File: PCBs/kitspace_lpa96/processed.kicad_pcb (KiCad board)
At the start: 4 copper layers, 143 x 74 mm, 161 parts, among them IC1 ATMEGA328-A, P1 CONN_2, P2 CONN_3X2, SW1 SW_PUSH, U1 SD_CARD, U2 LD1117S33, U3 TLC5941, U4 TLC5941, U5 TLC5941, U6 TLC5941, U7 TLC5941, U8 TLC5941, Y1 RESONATEUR

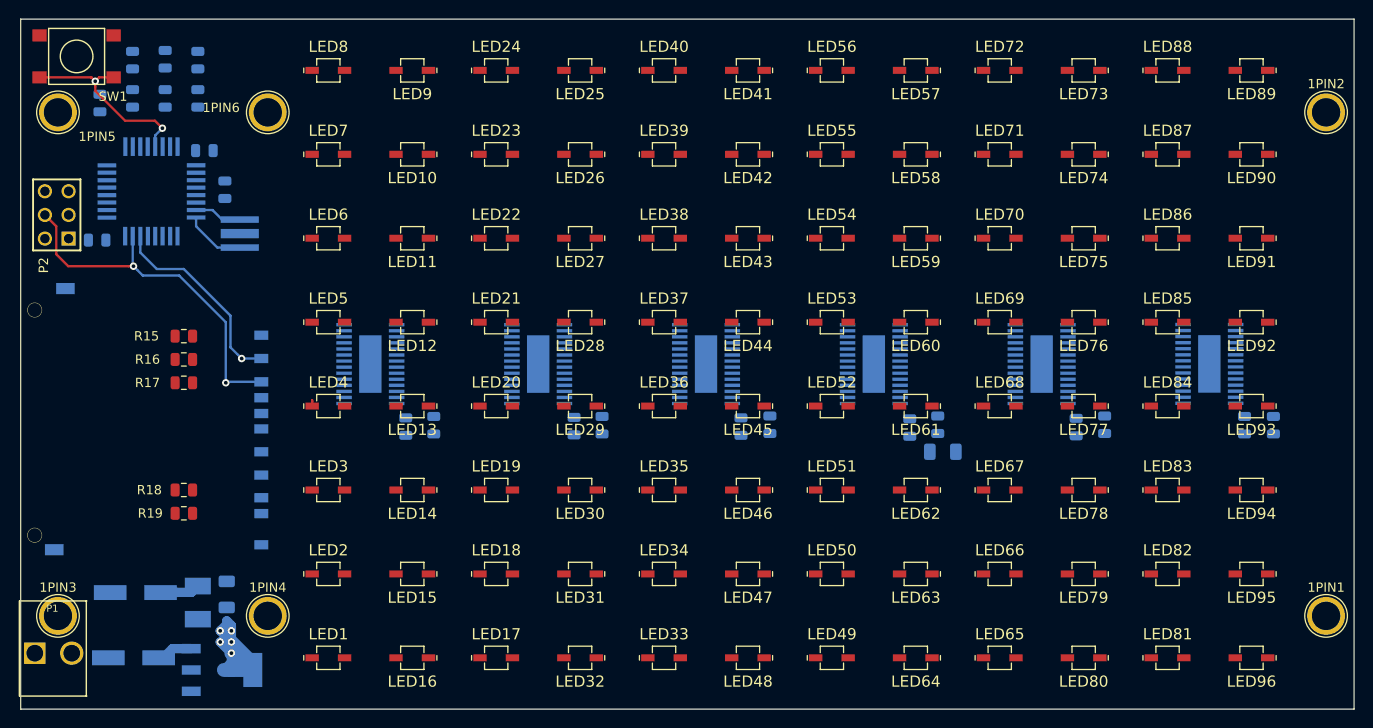
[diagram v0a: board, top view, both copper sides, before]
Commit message: recheck all circuits and clean up fill zone by rerouting the nets using freerouting and manually
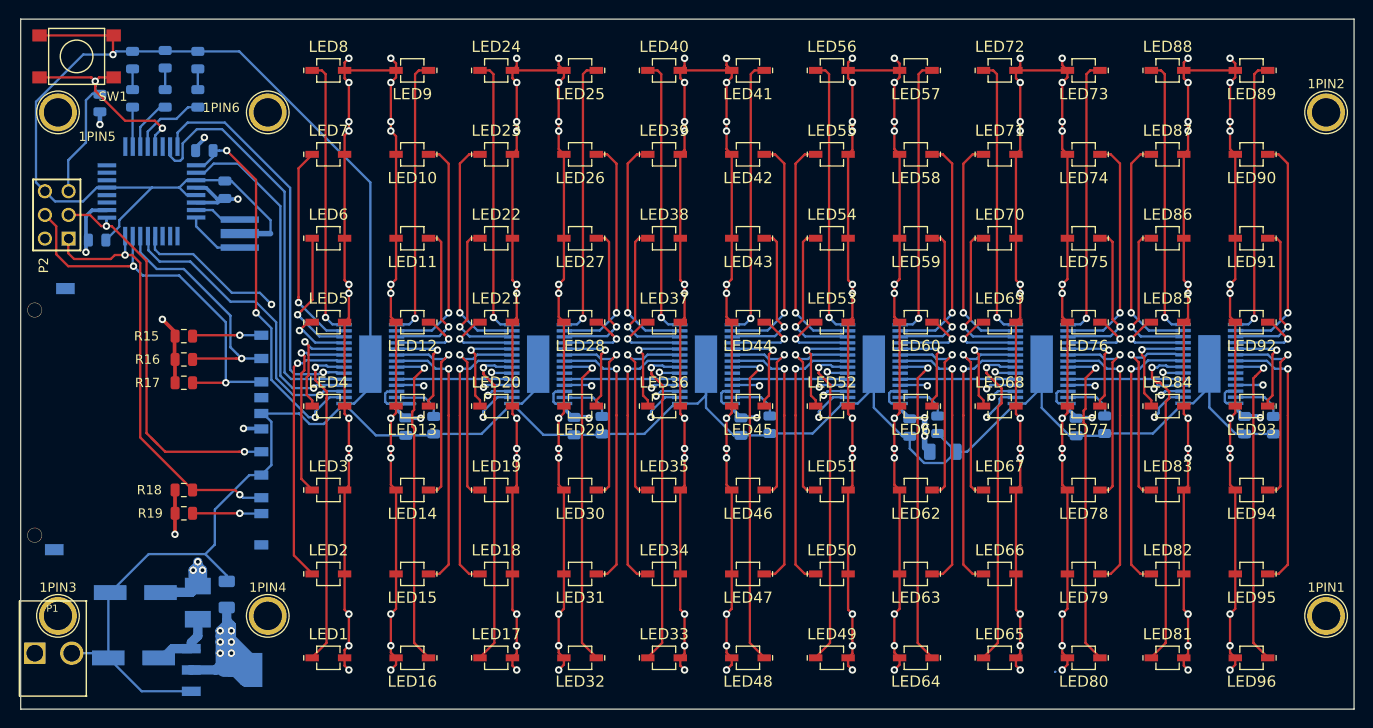
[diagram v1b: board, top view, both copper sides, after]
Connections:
- C1 pad 1: (no net) -> GND
- C1 pad 2: (no net) -> VCC
- C10 pad 1: (no net) -> VCC
- C10 pad 2: (no net) -> GND
- C11 pad 1: (no net) -> VCC
- C11 pad 2: (no net) -> GND
- C12 pad 1: (no net) -> VCC
- C12 pad 2: (no net) -> GND
- C2 pad 1: (no net) -> GND
- C2 pad 2: (no net) -> VCC
- C3 pad 2: (no net) -> GND
- C4 pad 2: (no net) -> GND
- C5 pad 1: (no net) -> VCC
- C5 pad 2: (no net) -> GND
- C6 pad 1: (no net) -> VCC
- C6 pad 2: (no net) -> GND
- C7 pad 1: (no net) -> VCC
- C7 pad 2: (no net) -> GND
- C8 pad 1: (no net) -> VCC
- C8 pad 2: (no net) -> GND
- C9 pad 1: (no net) -> VCC
- C9 pad 2: (no net) -> GND
- IC1 pad 1: (no net) -> /BLANK
- IC1 pad 10: (no net) -> Net-(IC1-Pad10)
- IC1 pad 11: (no net) -> Net-(IC1-Pad11)
- IC1 pad 12: (no net) -> /GSCLK
- IC1 pad 13: (no net) -> /XLAT
- IC1 pad 16: (no net) -> /MISO
- IC1 pad 17: (no net) -> /SCK
- IC1 pad 18: (no net) -> VCC
- IC1 pad 19: (no net) -> Net-(IC1-Pad19)
- IC1 pad 2: (no net) -> /SCLK
- IC1 pad 20: (no net) -> Net-(IC1-Pad20)
- IC1 pad 21: (no net) -> GND
- IC1 pad 22: (no net) -> Net-(IC1-Pad22)
- IC1 pad 23: (no net) -> Net-(IC1-Pad23)
- IC1 pad 24: (no net) -> Net-(IC1-Pad24)
- IC1 pad 25: (no net) -> Net-(IC1-Pad25)
- IC1 pad 26: (no net) -> /ON
- IC1 pad 27: (no net) -> /ERR
- IC1 pad 28: (no net) -> /FIN
- IC1 pad 3: (no net) -> GND
- IC1 pad 30: (no net) -> Net-(IC1-Pad30)
- IC1 pad 31: (no net) -> /SIN
- IC1 pad 32: (no net) -> /MODE
- IC1 pad 4: (no net) -> VCC
- IC1 pad 5: (no net) -> GND
- IC1 pad 6: (no net) -> VCC
- IC1 pad 9: (no net) -> Net-(IC1-Pad9)
- L1 pad 2: (no net) -> Net-(C4-Pad1)
- LED1 pad 1: (no net) -> Net-(LED1-Pad1)
- LED1 pad 2: (no net) -> /VIN
- LED10 pad 1: (no net) -> Net-(LED10-Pad1)
- LED10 pad 2: (no net) -> /VIN
- LED11 pad 1: (no net) -> Net-(LED11-Pad1)
- LED11 pad 2: (no net) -> /VIN
- LED12 pad 1: (no net) -> Net-(LED12-Pad1)
- LED12 pad 2: (no net) -> /VIN
- LED13 pad 1: (no net) -> Net-(LED13-Pad1)
- LED13 pad 2: (no net) -> /VIN
- LED14 pad 1: (no net) -> Net-(LED14-Pad1)
- LED14 pad 2: (no net) -> /VIN
- LED15 pad 1: (no net) -> Net-(LED15-Pad1)
- LED15 pad 2: (no net) -> /VIN
- LED16 pad 1: (no net) -> Net-(LED16-Pad1)
- LED16 pad 2: (no net) -> /VIN
- LED17 pad 1: (no net) -> Net-(LED17-Pad1)
- LED17 pad 2: (no net) -> /VIN
- LED18 pad 1: (no net) -> Net-(LED18-Pad1)
- LED18 pad 2: (no net) -> /VIN
- LED19 pad 1: (no net) -> Net-(LED19-Pad1)
- LED19 pad 2: (no net) -> /VIN
- LED2 pad 1: (no net) -> Net-(LED2-Pad1)
- LED2 pad 2: (no net) -> /VIN
- LED20 pad 1: (no net) -> Net-(LED20-Pad1)
- LED20 pad 2: (no net) -> /VIN
- LED21 pad 1: (no net) -> Net-(LED21-Pad1)
- LED21 pad 2: (no net) -> /VIN
- LED22 pad 1: (no net) -> Net-(LED22-Pad1)
- LED22 pad 2: (no net) -> /VIN
- LED23 pad 1: (no net) -> Net-(LED23-Pad1)
- LED23 pad 2: (no net) -> /VIN
- LED24 pad 1: (no net) -> Net-(LED24-Pad1)
- LED24 pad 2: (no net) -> /VIN
- LED25 pad 1: (no net) -> Net-(LED25-Pad1)
- LED25 pad 2: (no net) -> /VIN
- LED26 pad 1: (no net) -> Net-(LED26-Pad1)
- LED26 pad 2: (no net) -> /VIN
- LED27 pad 1: (no net) -> Net-(LED27-Pad1)
- LED27 pad 2: (no net) -> /VIN
- LED28 pad 1: (no net) -> Net-(LED28-Pad1)
- LED28 pad 2: (no net) -> /VIN
- LED29 pad 1: (no net) -> Net-(LED29-Pad1)
- LED29 pad 2: (no net) -> /VIN
- LED3 pad 1: (no net) -> Net-(LED3-Pad1)
- LED3 pad 2: (no net) -> /VIN
- LED30 pad 1: (no net) -> Net-(LED30-Pad1)
- LED30 pad 2: (no net) -> /VIN
- LED31 pad 1: (no net) -> Net-(LED31-Pad1)
- LED31 pad 2: (no net) -> /VIN
- LED32 pad 1: (no net) -> Net-(LED32-Pad1)
- LED32 pad 2: (no net) -> /VIN
- LED33 pad 1: (no net) -> Net-(LED33-Pad1)
- LED33 pad 2: (no net) -> /VIN
- LED34 pad 1: (no net) -> Net-(LED34-Pad1)
- LED34 pad 2: (no net) -> /VIN
- LED35 pad 1: (no net) -> Net-(LED35-Pad1)
- LED35 pad 2: (no net) -> /VIN
- LED36 pad 1: (no net) -> Net-(LED36-Pad1)
- LED36 pad 2: (no net) -> /VIN
- LED37 pad 1: (no net) -> Net-(LED37-Pad1)
- LED37 pad 2: (no net) -> /VIN
- LED38 pad 1: (no net) -> Net-(LED38-Pad1)
- LED38 pad 2: (no net) -> /VIN
- LED39 pad 1: (no net) -> Net-(LED39-Pad1)
- LED39 pad 2: (no net) -> /VIN
- LED4 pad 2: (no net) -> /VIN
- LED40 pad 1: (no net) -> Net-(LED40-Pad1)
- LED40 pad 2: (no net) -> /VIN
- LED41 pad 1: (no net) -> Net-(LED41-Pad1)
- LED41 pad 2: (no net) -> /VIN
- LED42 pad 1: (no net) -> Net-(LED42-Pad1)
- LED42 pad 2: (no net) -> /VIN
- LED43 pad 1: (no net) -> Net-(LED43-Pad1)
- LED43 pad 2: (no net) -> /VIN
- LED44 pad 1: (no net) -> Net-(LED44-Pad1)
- LED44 pad 2: (no net) -> /VIN
- LED45 pad 1: (no net) -> Net-(LED45-Pad1)
- LED45 pad 2: (no net) -> /VIN
- LED46 pad 1: (no net) -> Net-(LED46-Pad1)
- LED46 pad 2: (no net) -> /VIN
- LED47 pad 1: (no net) -> Net-(LED47-Pad1)
- LED47 pad 2: (no net) -> /VIN
- LED48 pad 1: (no net) -> Net-(LED48-Pad1)
- LED48 pad 2: (no net) -> /VIN
- LED49 pad 1: (no net) -> Net-(LED49-Pad1)
- LED49 pad 2: (no net) -> /VIN
- LED5 pad 1: (no net) -> Net-(LED5-Pad1)
- LED5 pad 2: (no net) -> /VIN
- LED50 pad 1: (no net) -> Net-(LED50-Pad1)
- LED50 pad 2: (no net) -> /VIN
- LED51 pad 1: (no net) -> Net-(LED51-Pad1)
- LED51 pad 2: (no net) -> /VIN
- LED52 pad 1: (no net) -> Net-(LED52-Pad1)
- LED52 pad 2: (no net) -> /VIN
- LED53 pad 1: (no net) -> Net-(LED53-Pad1)
- LED53 pad 2: (no net) -> /VIN
- LED54 pad 1: (no net) -> Net-(LED54-Pad1)
- LED54 pad 2: (no net) -> /VIN
- LED55 pad 1: (no net) -> Net-(LED55-Pad1)
- LED55 pad 2: (no net) -> /VIN
- LED56 pad 1: (no net) -> Net-(LED56-Pad1)
- LED56 pad 2: (no net) -> /VIN
- LED57 pad 1: (no net) -> Net-(LED57-Pad1)
- LED57 pad 2: (no net) -> /VIN
- LED58 pad 1: (no net) -> Net-(LED58-Pad1)
- LED58 pad 2: (no net) -> /VIN
- LED59 pad 1: (no net) -> Net-(LED59-Pad1)
- LED59 pad 2: (no net) -> /VIN
- LED6 pad 1: (no net) -> Net-(LED6-Pad1)
- LED6 pad 2: (no net) -> /VIN
- LED60 pad 1: (no net) -> Net-(LED60-Pad1)
- LED60 pad 2: (no net) -> /VIN
- LED61 pad 1: (no net) -> Net-(LED61-Pad1)
- LED61 pad 2: (no net) -> /VIN
- LED62 pad 1: (no net) -> Net-(LED62-Pad1)
- LED62 pad 2: (no net) -> /VIN
- LED63 pad 1: (no net) -> Net-(LED63-Pad1)
- LED63 pad 2: (no net) -> /VIN
- LED64 pad 1: (no net) -> Net-(LED64-Pad1)
- LED64 pad 2: (no net) -> /VIN
- LED65 pad 1: (no net) -> Net-(LED65-Pad1)
- LED65 pad 2: (no net) -> /VIN
- LED66 pad 1: (no net) -> Net-(LED66-Pad1)
- LED66 pad 2: (no net) -> /VIN
- LED67 pad 1: (no net) -> Net-(LED67-Pad1)
- LED67 pad 2: (no net) -> /VIN
- LED68 pad 1: (no net) -> Net-(LED68-Pad1)
- LED68 pad 2: (no net) -> /VIN
- LED69 pad 1: (no net) -> Net-(LED69-Pad1)
- LED69 pad 2: (no net) -> /VIN
- LED7 pad 1: (no net) -> Net-(LED7-Pad1)
- LED7 pad 2: (no net) -> /VIN
- LED70 pad 1: (no net) -> Net-(LED70-Pad1)
- LED70 pad 2: (no net) -> /VIN
- LED71 pad 1: (no net) -> Net-(LED71-Pad1)
- LED71 pad 2: (no net) -> /VIN
- LED72 pad 1: (no net) -> Net-(LED72-Pad1)
- LED72 pad 2: (no net) -> /VIN
- LED73 pad 1: (no net) -> Net-(LED73-Pad1)
- LED73 pad 2: (no net) -> /VIN
- LED74 pad 1: (no net) -> Net-(LED74-Pad1)
- LED74 pad 2: (no net) -> /VIN
- LED75 pad 1: (no net) -> Net-(LED75-Pad1)
- LED75 pad 2: (no net) -> /VIN
- LED76 pad 1: (no net) -> Net-(LED76-Pad1)
- LED76 pad 2: (no net) -> /VIN
- LED77 pad 1: (no net) -> Net-(LED77-Pad1)
- LED77 pad 2: (no net) -> /VIN
- LED78 pad 1: (no net) -> Net-(LED78-Pad1)
- LED78 pad 2: (no net) -> /VIN
- LED79 pad 1: (no net) -> Net-(LED79-Pad1)
- LED79 pad 2: (no net) -> /VIN
- LED8 pad 1: (no net) -> Net-(LED8-Pad1)
- LED8 pad 2: (no net) -> /VIN
- LED80 pad 1: (no net) -> Net-(LED80-Pad1)
- LED80 pad 2: (no net) -> /VIN
- LED81 pad 1: (no net) -> Net-(LED81-Pad1)
- LED81 pad 2: (no net) -> /VIN
- LED82 pad 1: (no net) -> Net-(LED82-Pad1)
- LED82 pad 2: (no net) -> /VIN
- LED83 pad 1: (no net) -> Net-(LED83-Pad1)
- LED83 pad 2: (no net) -> /VIN
- LED84 pad 1: (no net) -> Net-(LED84-Pad1)
- LED84 pad 2: (no net) -> /VIN
- LED85 pad 1: (no net) -> Net-(LED85-Pad1)
- LED85 pad 2: (no net) -> /VIN
- LED86 pad 1: (no net) -> Net-(LED86-Pad1)
- LED86 pad 2: (no net) -> /VIN
- LED87 pad 1: (no net) -> Net-(LED87-Pad1)
- LED87 pad 2: (no net) -> /VIN
- LED88 pad 1: (no net) -> Net-(LED88-Pad1)
- LED88 pad 2: (no net) -> /VIN
- LED89 pad 1: (no net) -> Net-(LED89-Pad1)
- LED89 pad 2: (no net) -> /VIN
- LED9 pad 1: (no net) -> Net-(LED9-Pad1)
- LED9 pad 2: (no net) -> /VIN
- LED90 pad 1: (no net) -> Net-(LED90-Pad1)
- LED90 pad 2: (no net) -> /VIN
- LED91 pad 1: (no net) -> Net-(LED91-Pad1)
- LED91 pad 2: (no net) -> /VIN
- LED92 pad 1: (no net) -> Net-(LED92-Pad1)
- LED92 pad 2: (no net) -> /VIN
- LED93 pad 1: (no net) -> Net-(LED93-Pad1)
- LED93 pad 2: (no net) -> /VIN
- LED94 pad 1: (no net) -> Net-(LED94-Pad1)
- LED94 pad 2: (no net) -> /VIN
- LED95 pad 1: (no net) -> Net-(LED95-Pad1)
- LED95 pad 2: (no net) -> /VIN
- LED96 pad 1: (no net) -> Net-(LED96-Pad1)
- LED96 pad 2: (no net) -> /VIN
- LED97 pad 1: (no net) -> GND
- LED97 pad 2: (no net) -> Net-(LED97-Pad2)
- LED98 pad 1: (no net) -> GND
- LED98 pad 2: (no net) -> Net-(LED98-Pad2)
- LED99 pad 1: (no net) -> GND
- LED99 pad 2: (no net) -> Net-(LED99-Pad2)
- P1 pad 1: (no net) -> /VIN
- P1 pad 2: (no net) -> GND
- P2 pad 1: (no net) -> /MISO
- P2 pad 2: (no net) -> VCC
- P2 pad 3: (no net) -> /SCK
- P2 pad 5: (no net) -> /RST
- P2 pad 6: (no net) -> GND
- R1 pad 1: (no net) -> /RST
- R1 pad 2: (no net) -> VCC
- R10 pad 1: (no net) -> /ERR
- R10 pad 2: (no net) -> Net-(LED98-Pad2)
- R11 pad 1: (no net) -> /FIN
- R11 pad 2: (no net) -> Net-(LED99-Pad2)
- R15 pad 1: (no net) -> VCC
- R15 pad 2: (no net) -> Net-(R15-Pad2)
- R16 pad 1: (no net) -> VCC
- R16 pad 2: (no net) -> /SS
- R17 pad 1: (no net) -> VCC
- R17 pad 2: (no net) -> /MOSI
- R18 pad 1: (no net) -> VCC
- R18 pad 2: (no net) -> /MISO
- R19 pad 1: (no net) -> VCC
- R19 pad 2: (no net) -> Net-(R19-Pad2)
- R2 pad 1: (no net) -> /BLANK
- R2 pad 2: (no net) -> VCC
- R3 pad 1: (no net) -> GND
- R3 pad 2: (no net) -> Net-(R3-Pad2)
- R4 pad 1: (no net) -> GND
- R4 pad 2: (no net) -> Net-(R4-Pad2)
- R5 pad 1: (no net) -> GND
- R5 pad 2: (no net) -> Net-(R5-Pad2)
- R6 pad 1: (no net) -> GND
- R6 pad 2: (no net) -> Net-(R6-Pad2)
- R7 pad 1: (no net) -> GND
- R7 pad 2: (no net) -> Net-(R7-Pad2)
- R8 pad 1: (no net) -> GND
- R8 pad 2: (no net) -> Net-(R8-Pad2)
- R9 pad 1: (no net) -> /ON
- R9 pad 2: (no net) -> Net-(LED97-Pad2)
- SW1 pad 2: (no net) -> GND
- U1 pad 3: (no net) -> GND
- U1 pad 4: (no net) -> VCC
- U1 pad 5: (no net) -> /SCK
- U1 pad 6: (no net) -> GND
- U1 pad 7: (no net) -> /MISO
- U1 pad 8: (no net) -> Net-(R19-Pad2)
- U1 pad 9: (no net) -> Net-(R15-Pad2)
- U2 pad 1: (no net) -> GND
- U2 pad 2: (no net) -> VCC
- U3 pad 1: (no net) -> GND
- U3 pad 10: (no net) -> Net-(LED4-Pad1)
- U3 pad 11: (no net) -> Net-(LED5-Pad1)
- U3 pad 12: (no net) -> Net-(LED6-Pad1)
- U3 pad 13: (no net) -> Net-(LED7-Pad1)
- U3 pad 14: (no net) -> Net-(LED8-Pad1)
- U3 pad 15: (no net) -> Net-(LED9-Pad1)
- U3 pad 16: (no net) -> Net-(LED10-Pad1)
- U3 pad 17: (no net) -> Net-(LED11-Pad1)
- U3 pad 18: (no net) -> Net-(LED12-Pad1)
- U3 pad 19: (no net) -> Net-(LED13-Pad1)
- U3 pad 2: (no net) -> /BLANK
- U3 pad 20: (no net) -> Net-(LED14-Pad1)
- U3 pad 21: (no net) -> Net-(LED15-Pad1)
- U3 pad 22: (no net) -> Net-(LED16-Pad1)
- U3 pad 23: (no net) -> Net-(U3-Pad23)
- U3 pad 24: (no net) -> /lpa96_leds_drivers/SOUT1
- U3 pad 25: (no net) -> /GSCLK
- U3 pad 26: (no net) -> VCC
- U3 pad 27: (no net) -> Net-(R3-Pad2)
- U3 pad 28: (no net) -> VCC
- U3 pad 29: (no net) -> GND
- U3 pad 3: (no net) -> /XLAT
- U3 pad 4: (no net) -> /SCLK
- U3 pad 5: (no net) -> /SIN
- U3 pad 6: (no net) -> /MODE
- U3 pad 7: (no net) -> Net-(LED1-Pad1)
- U3 pad 8: (no net) -> Net-(LED2-Pad1)
- U3 pad 9: (no net) -> Net-(LED3-Pad1)
- U4 pad 1: (no net) -> GND
- U4 pad 10: (no net) -> Net-(LED20-Pad1)
- U4 pad 11: (no net) -> Net-(LED21-Pad1)
- U4 pad 12: (no net) -> Net-(LED22-Pad1)
- U4 pad 13: (no net) -> Net-(LED23-Pad1)
- U4 pad 14: (no net) -> Net-(LED24-Pad1)
- U4 pad 15: (no net) -> Net-(LED25-Pad1)
- U4 pad 16: (no net) -> Net-(LED26-Pad1)
- U4 pad 17: (no net) -> Net-(LED27-Pad1)
- U4 pad 18: (no net) -> Net-(LED28-Pad1)
- U4 pad 19: (no net) -> Net-(LED29-Pad1)
- U4 pad 2: (no net) -> /BLANK
- U4 pad 20: (no net) -> Net-(LED30-Pad1)
- U4 pad 21: (no net) -> Net-(LED31-Pad1)
- U4 pad 22: (no net) -> Net-(LED32-Pad1)
- U4 pad 23: (no net) -> Net-(U4-Pad23)
- U4 pad 24: (no net) -> /lpa96_leds_drivers/SOUT2
- U4 pad 25: (no net) -> /GSCLK
- U4 pad 26: (no net) -> VCC
- U4 pad 27: (no net) -> Net-(R4-Pad2)
- U4 pad 28: (no net) -> VCC
- U4 pad 29: (no net) -> GND
- U4 pad 3: (no net) -> /XLAT
- U4 pad 4: (no net) -> /SCLK
- U4 pad 5: (no net) -> /lpa96_leds_drivers/SOUT1
- U4 pad 6: (no net) -> /MODE
- U4 pad 7: (no net) -> Net-(LED17-Pad1)
- U4 pad 8: (no net) -> Net-(LED18-Pad1)
- U4 pad 9: (no net) -> Net-(LED19-Pad1)
- U5 pad 1: (no net) -> GND
- U5 pad 10: (no net) -> Net-(LED36-Pad1)
- U5 pad 11: (no net) -> Net-(LED37-Pad1)
- U5 pad 12: (no net) -> Net-(LED38-Pad1)
- U5 pad 13: (no net) -> Net-(LED39-Pad1)
- U5 pad 14: (no net) -> Net-(LED40-Pad1)
- U5 pad 15: (no net) -> Net-(LED41-Pad1)
- U5 pad 16: (no net) -> Net-(LED42-Pad1)
- U5 pad 17: (no net) -> Net-(LED43-Pad1)
- U5 pad 18: (no net) -> Net-(LED44-Pad1)
- U5 pad 19: (no net) -> Net-(LED45-Pad1)
- U5 pad 2: (no net) -> /BLANK
- U5 pad 20: (no net) -> Net-(LED46-Pad1)
- U5 pad 21: (no net) -> Net-(LED47-Pad1)
- U5 pad 22: (no net) -> Net-(LED48-Pad1)
- U5 pad 23: (no net) -> Net-(U5-Pad23)
- U5 pad 24: (no net) -> /lpa96_leds_drivers/SOUT3
- U5 pad 25: (no net) -> /GSCLK
- U5 pad 26: (no net) -> VCC
- U5 pad 27: (no net) -> Net-(R5-Pad2)
- U5 pad 28: (no net) -> VCC
- U5 pad 29: (no net) -> GND
- U5 pad 3: (no net) -> /XLAT
- U5 pad 4: (no net) -> /SCLK
- U5 pad 5: (no net) -> /lpa96_leds_drivers/SOUT2
- U5 pad 6: (no net) -> /MODE
- U5 pad 7: (no net) -> Net-(LED33-Pad1)
- U5 pad 8: (no net) -> Net-(LED34-Pad1)
- U5 pad 9: (no net) -> Net-(LED35-Pad1)
- U6 pad 1: (no net) -> GND
- U6 pad 10: (no net) -> Net-(LED52-Pad1)
- U6 pad 11: (no net) -> Net-(LED53-Pad1)
- U6 pad 12: (no net) -> Net-(LED54-Pad1)
- U6 pad 13: (no net) -> Net-(LED55-Pad1)
- U6 pad 14: (no net) -> Net-(LED56-Pad1)
- U6 pad 15: (no net) -> Net-(LED57-Pad1)
- U6 pad 16: (no net) -> Net-(LED58-Pad1)
- U6 pad 17: (no net) -> Net-(LED59-Pad1)
- U6 pad 18: (no net) -> Net-(LED60-Pad1)
- U6 pad 19: (no net) -> Net-(LED61-Pad1)
- U6 pad 2: (no net) -> /BLANK
- U6 pad 20: (no net) -> Net-(LED62-Pad1)
- U6 pad 21: (no net) -> Net-(LED63-Pad1)
- U6 pad 22: (no net) -> Net-(LED64-Pad1)
- U6 pad 23: (no net) -> Net-(U6-Pad23)
- U6 pad 24: (no net) -> /lpa96_leds_drivers/SOUT4
- U6 pad 25: (no net) -> /GSCLK
- U6 pad 26: (no net) -> VCC
- U6 pad 27: (no net) -> Net-(R6-Pad2)
- U6 pad 28: (no net) -> VCC
- U6 pad 29: (no net) -> GND
- U6 pad 3: (no net) -> /XLAT
- U6 pad 4: (no net) -> /SCLK
- U6 pad 5: (no net) -> /lpa96_leds_drivers/SOUT3
- U6 pad 6: (no net) -> /MODE
- U6 pad 7: (no net) -> Net-(LED49-Pad1)
- U6 pad 8: (no net) -> Net-(LED50-Pad1)
- U6 pad 9: (no net) -> Net-(LED51-Pad1)
- U7 pad 1: (no net) -> GND
- U7 pad 10: (no net) -> Net-(LED68-Pad1)
- U7 pad 11: (no net) -> Net-(LED69-Pad1)
- U7 pad 12: (no net) -> Net-(LED70-Pad1)
- U7 pad 13: (no net) -> Net-(LED71-Pad1)
- U7 pad 14: (no net) -> Net-(LED72-Pad1)
- U7 pad 15: (no net) -> Net-(LED73-Pad1)
- U7 pad 16: (no net) -> Net-(LED74-Pad1)
- U7 pad 17: (no net) -> Net-(LED75-Pad1)
- U7 pad 18: (no net) -> Net-(LED76-Pad1)
- U7 pad 19: (no net) -> Net-(LED77-Pad1)
- U7 pad 2: (no net) -> /BLANK
- U7 pad 20: (no net) -> Net-(LED78-Pad1)
- U7 pad 21: (no net) -> Net-(LED79-Pad1)
- U7 pad 22: (no net) -> Net-(LED80-Pad1)
- U7 pad 23: (no net) -> Net-(U7-Pad23)
- U7 pad 24: (no net) -> /lpa96_leds_drivers/SOUT5
- U7 pad 25: (no net) -> /GSCLK
- U7 pad 26: (no net) -> VCC
- U7 pad 27: (no net) -> Net-(R7-Pad2)
- U7 pad 28: (no net) -> VCC
- U7 pad 29: (no net) -> GND
- U7 pad 3: (no net) -> /XLAT
- U7 pad 4: (no net) -> /SCLK
- U7 pad 5: (no net) -> /lpa96_leds_drivers/SOUT4
- U7 pad 6: (no net) -> /MODE
- U7 pad 7: (no net) -> Net-(LED65-Pad1)
- U7 pad 8: (no net) -> Net-(LED66-Pad1)
- U7 pad 9: (no net) -> Net-(LED67-Pad1)
- U8 pad 1: (no net) -> GND
- U8 pad 10: (no net) -> Net-(LED84-Pad1)
- U8 pad 11: (no net) -> Net-(LED85-Pad1)
- U8 pad 12: (no net) -> Net-(LED86-Pad1)
- U8 pad 13: (no net) -> Net-(LED87-Pad1)
- U8 pad 14: (no net) -> Net-(LED88-Pad1)
- U8 pad 15: (no net) -> Net-(LED89-Pad1)
- U8 pad 16: (no net) -> Net-(LED90-Pad1)
- U8 pad 17: (no net) -> Net-(LED91-Pad1)
- U8 pad 18: (no net) -> Net-(LED92-Pad1)
- U8 pad 19: (no net) -> Net-(LED93-Pad1)
- U8 pad 2: (no net) -> /BLANK
- U8 pad 20: (no net) -> Net-(LED94-Pad1)
- U8 pad 21: (no net) -> Net-(LED95-Pad1)
- U8 pad 22: (no net) -> Net-(LED96-Pad1)
- U8 pad 23: (no net) -> Net-(U8-Pad23)
- U8 pad 24: (no net) -> /lpa96_leds_drivers/SOUT
- U8 pad 25: (no net) -> /GSCLK
- U8 pad 26: (no net) -> VCC
- U8 pad 27: (no net) -> Net-(R8-Pad2)
- U8 pad 28: (no net) -> VCC
- U8 pad 29: (no net) -> GND
- U8 pad 3: (no net) -> /XLAT
- U8 pad 4: (no net) -> /SCLK
- U8 pad 5: (no net) -> /lpa96_leds_drivers/SOUT5
- U8 pad 6: (no net) -> /MODE
- U8 pad 7: (no net) -> Net-(LED81-Pad1)
- U8 pad 8: (no net) -> Net-(LED82-Pad1)
- U8 pad 9: (no net) -> Net-(LED83-Pad1)
- Y1 pad 2: (no net) -> GND
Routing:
- net /VIN: track 4.29 -> 1087.9 mm, vias 0 -> 147
- net GND: track 0.00 -> 356.9 mm, vias 0 -> 1
- net VCC: track 21.9 -> 346.2 mm, vias 5 -> 21
- net /BLANK: track 0.00 -> 152.6 mm, vias 0 -> 8
- net /GSCLK: track 0.00 -> 144.7 mm, vias 0 -> 7
- net /MODE: track 0.00 -> 140.9 mm, vias 0 -> 6
- net /SCLK: track 0.00 -> 140.8 mm, vias 0 -> 6
- net /XLAT: track 0.00 -> 134.0 mm, vias 0 -> 6
- net /MISO: track 0.00 -> 47.1 mm, vias 0 -> 2
- net /SCK: track 0.00 -> 44.2 mm, vias 0 -> 2
- net /SIN: track 0.00 -> 44.1 mm
- net Net-(LED81-Pad1): track 0.00 -> 35.7 mm, vias 0 -> 1
- net Net-(LED65-Pad1): track 0.00 -> 35.2 mm, vias 0 -> 1
- net Net-(LED49-Pad1): track 0.00 -> 34.9 mm, vias 0 -> 1
- net Net-(LED1-Pad1): track 0.00 -> 34.8 mm, vias 0 -> 1
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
